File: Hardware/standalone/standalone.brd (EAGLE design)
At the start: 100 x 80 mm, 98 parts, among them IC1 STM32F050C6T6A, IC2 AP1212, IC3 IR2104S, Q1 32.768khz, U10 ZXCT1107SA-7, U11 NMOS_2N7002, U12 NMOS_2N7002, U2 FDS6690a, U3 FDS6690a, U4 LM2576S, U5 NMOS_2N7002, U6 NMOS_2N7002, U7 INA213AIDCKT, U8 NMOS_2N7002, U9 PMOS_RSS090P03, X1 KUSBVX, X2 KUSBVX

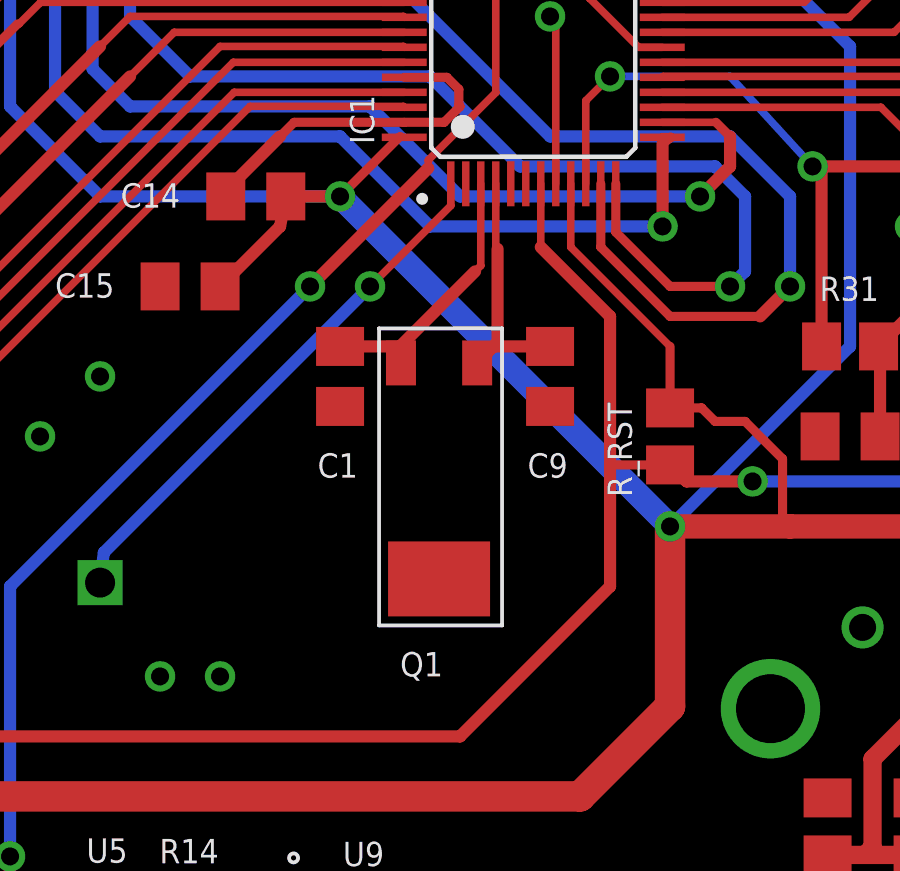
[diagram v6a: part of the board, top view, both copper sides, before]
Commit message: Changed RTC XTAL Hardware
Both Home and Pro boards have working XTAL. OC_FARNELL attributes give
correct part numbers.
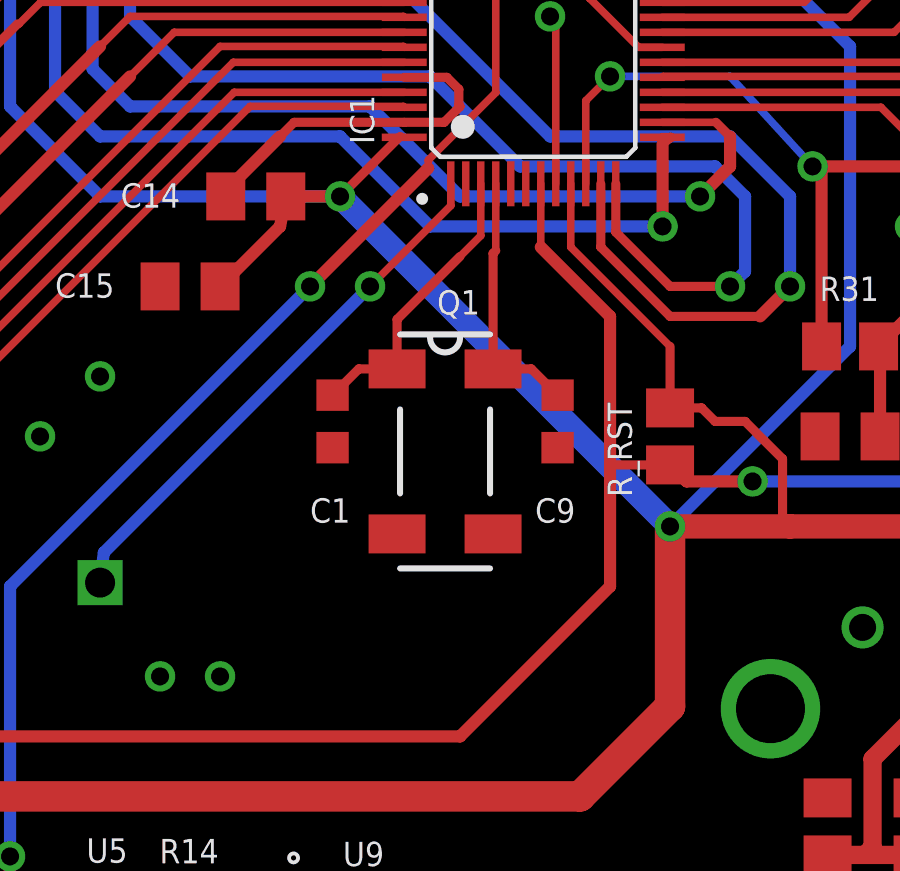
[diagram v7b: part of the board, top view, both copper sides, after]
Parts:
- C1, C9: value 12.5pF -> 6.8pF; device resistor:C0805K -> resistor:C0603K
- Q1: value 32.768khz -> 32.768kHz; device equinox:CRYSTAL_CMJ206T -> crystal:MC-306
- moved C1 1.52 mm to (31.8, 32.5)
- moved C9 1.52 mm to (39.2, 32.5)
- moved Q1 0.71 mm to (35.5, 31.5), turned to 270 degrees
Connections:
- net GND: no longer Q1.CASE
- net N$1: now also Q1.1; no longer Q1.P$2
- net N$18: now also Q1.4; no longer Q1.P$3
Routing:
- net N$1: track 9.10 -> 9.84 mm
- net N$18: track 8.16 -> 8.72 mm

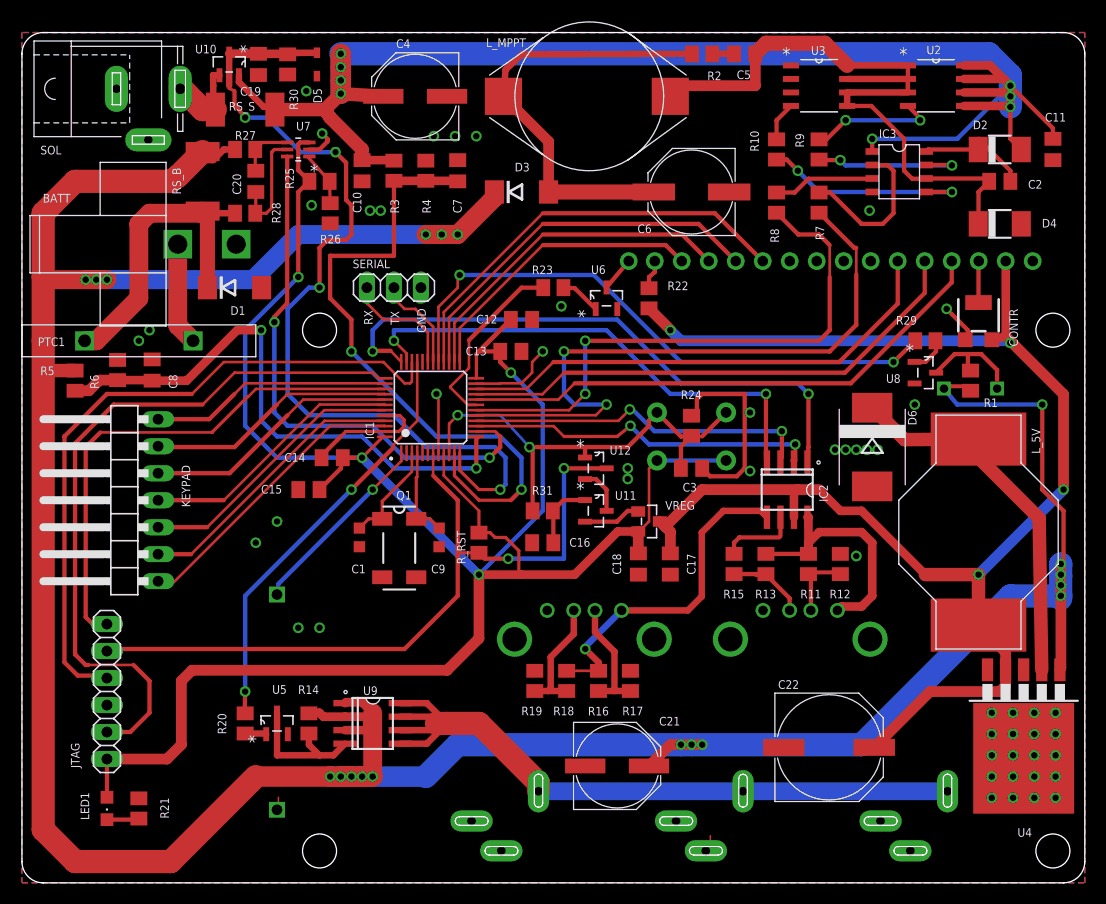
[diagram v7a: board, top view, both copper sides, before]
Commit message: izuba.box home production data added
This production data will be used to obtain a quote for assembly from
quick-tech.
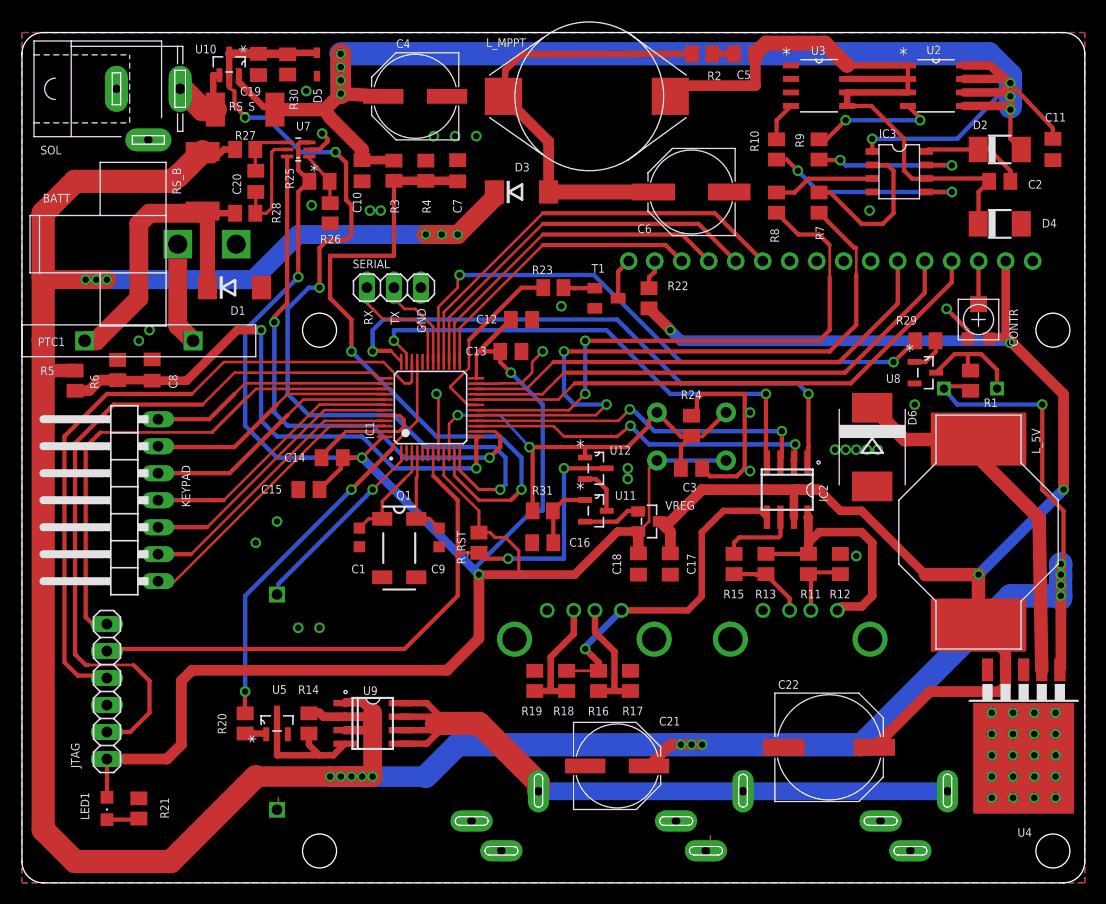
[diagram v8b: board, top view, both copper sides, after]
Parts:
- removed U6: NMOS_2N7002, equinox:SOT103P240X110-3N
- added T1: (no value), transistor:SOT23-BEC
- CONTR: device resistor:RTRIM3304W -> equinox:R_TRIMM_RC33X
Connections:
- net +5V: now also CONTR.CW; no longer CONTR.3
- net GND: now also CONTR.CCW, T1.E; no longer CONTR.1, U6.2
- net N$2: now also CONTR.WIPE; no longer CONTR.2
- net N$31: now also T1.C; no longer U6.3
- net N$32: now also T1.B; no longer U6.1
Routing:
- net N$32: track 3.85 -> 2.95 mm
- net N$31: track 3.25 -> 4.04 mm
